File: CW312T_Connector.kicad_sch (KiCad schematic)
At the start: 1 part, among them P1 PCIEx4 EDGE CONNECTOR

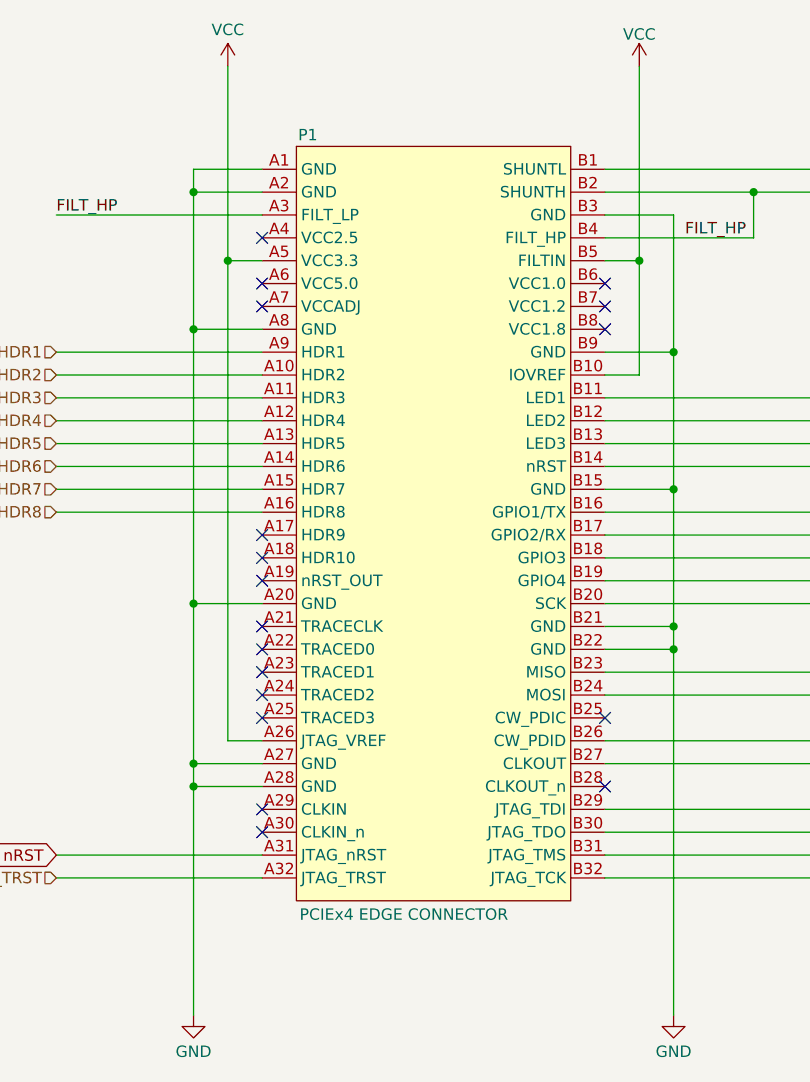
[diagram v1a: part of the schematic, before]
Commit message: updated schematic and pcb after library re-organization
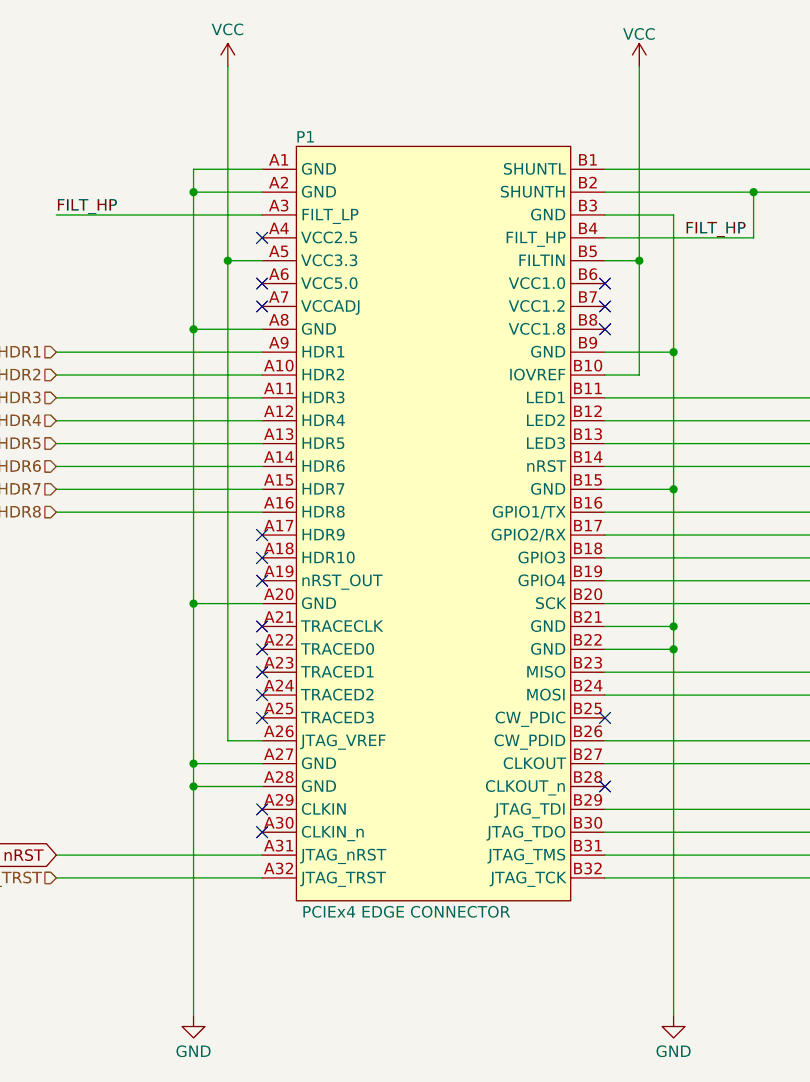
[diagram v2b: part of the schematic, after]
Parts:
- removed P1: PCIEx4 EDGE CONNECTOR, tutorial_2_library:CW312_Template, symbol tutorial_2_library:CW312T-Template
- added P1: PCIEx4 EDGE CONNECTOR, tutorial_2_library:CW312_Template, symbol NAE_Connectors:CW312T-Template
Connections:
- net CLKIN: now also P1.B27 (CLKOUT)
- net CS: now also P1.B26 (CW_PDID)
- net GND: now also P1.A1 (GND), P1.A2 (GND), P1.A20 (GND), P1.A27 (GND), P1.A28 (GND), P1.A8 (GND), P1.B15 (GND), P1.B21 (GND), P1.B22 (GND), P1.B3 (GND), P1.B9 (GND)
- net GPIO1_TX: now also P1.B16 (GPIO1/TX)
- net GPIO2_RX: now also P1.B17 (GPIO2/RX)
- net GPIO3: now also P1.B18 (GPIO3)
- net GPIO4: now also P1.B19 (GPIO4)
- net HDR1: now also P1.A9 (HDR1)
- net HDR2: now also P1.A10 (HDR2)
- net HDR3: now also P1.A11 (HDR3)
- net HDR4: now also P1.A12 (HDR4)
- net HDR5: now also P1.A13 (HDR5)
- net HDR6: now also P1.A14 (HDR6)
- net HDR7: now also P1.A15 (HDR7)
- net HDR8: now also P1.A16 (HDR8)
- net JTAG_TCK: now also P1.B32 (JTAG_TCK)
- net JTAG_TDI: now also P1.B29 (JTAG_TDI)
- net JTAG_TDO: now also P1.B30 (JTAG_TDO)
- net JTAG_TMS: now also P1.B31 (JTAG_TMS)
- net JTAG_TRST: now also P1.A32 (JTAG_TRST)
- net LED1: now also P1.B11 (LED1)
- net LED2: now also P1.B12 (LED2)
- net LED3: now also P1.B13 (LED3)
- net MISO: now also P1.B23 (MISO)
- net MOSI: now also P1.B24 (MOSI)
- net SCK: now also P1.B20 (SCK)
- net SHUNTH: now also P1.A3 (FILT_LP), P1.B2 (SHUNTH), P1.B4 (FILT_HP)
- net SHUNTL: now also P1.B1 (SHUNTL)
- net VCC: now also P1.A26 (JTAG_VREF), P1.A5 (VCC3.3), P1.B10 (IOVREF), P1.B5 (FILTIN)
- net nRST: now also P1.A31 (JTAG_nRST), P1.B14 (nRST)
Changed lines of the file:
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@@
+	)
+	(symbol
+		(lib_id "NAE_Connectors:CW312T-Template")
+		(at 128.27 49.53 0)
+		(unit 1)
+		(exclude_from_sim no)
+		(in_bom no)
+		(on_board yes)
+		(dnp no)
+		(property "Reference" "P1"
+			(at 114.046 45.974 0)
+			(effects
+				(font
+					(size 1.27 1.27)
+				)
+			)
+		)
+		(property "Value" "PCIEx4 EDGE CONNECTOR"
+			(at 125.222 132.08 0)
+			(effects
+				(font
+					(size 1.27 1.27)
+				)
+			)
+		)
+		(property "Footprint" "tutorial_2_library:CW312_Template"
+			(at 124.46 142.24 0)
+			(effects
+				(font
+					(size 1.27 1.27)
+				)
+				(hide yes)
+			)
+		)
+		(property "Datasheet" ""
+			(at 125.73 48.26 0)
+			(effects
+				(font
+					(size 1.27 1.27)
+				)
+				(hide yes)
+			)
+		)
+		(property "Description" "BOARD AND EDGE CONNECTOR TEMPLATE FOR CW312 TARGETS"
+			(at 137.16 138.43 0)
+			(effects
+				(font
+					(size 1.27 1.27)
+				)
+				(hide yes)
+			)
+		)
+		(pin "A18"
+		)
+		(pin "A20"
+		)
+		(pin "A24"
+		)
+		(pin "A19"
+		)
+		(pin "A11"
+		)
+		(pin "A2"
+		)
+		(pin "A17"
+		)
+		(pin "A25"
+		)
+		(pin "A27"
+		)
+		(pin "A21"
+		)
+		(pin "A28"
+		)
+		(pin "A29"
+		)
+		(pin "A3"
+		)
+		(pin "A30"
+		)
+		(pin "A31"
+		)
+		(pin "A13"
+		)
+		(pin "A32"
+		)
+		(pin "A4"
+		)
+		(pin "A22"
+		)
+		(pin "A23"
+		)
+		(pin "A26"
+		)
+		(pin "A5"
+		)
+		(pin "A6"
+		)
+		(pin "B2"
+		)
+		(pin "A10"
+		)
+		(pin "A1"
+		)
+		(pin "A12"
+		)
+		(pin "A14"
+		)
+		(pin "A15"
+		)
+		(pin "A16"
+		)
+		(pin "A7"
+		)
+		(pin "B31"
+		)
+		(pin "B7"
+		)
+		(pin "B24"
+		)
+		(pin "B17"
+		)
+		(pin "B12"
+		)
+		(pin "B29"
+		)
+		(pin "B13"
+		)
+		(pin "B4"
+		)
+		(pin "B6"
+		)
+		(pin "B15"
+		)
+		(pin "B23"
+		)
+		(pin "B27"
+		)
+		(pin "B18"
+		)
+		(pin "B11"
+		)
+		(pin "B28"
+		)
+		(pin "A9"
+		)
+		(pin "B14"
+		)
+		(pin "B21"
+		)
+		(pin "B25"
+		)
+		(pin "B26"
+		)
+		(pin "B5"
+		)
+		(pin "B22"
+		)
+		(pin "B8"
+		)
+		(pin "B9"
+		)
+		(pin "B16"
+		)
+		(pin "B20"
+		)
+		(pin "A8"
+		)
+		(pin "B1"
+		)
+		(pin "B19"
+		)
+		(pin "B3"
+		)
+		(pin "B10"
+		)
+		(pin "B30"
+		)
+		(pin "B32"
+		)
+		(instances
+			(project ""
+				(path "/ece4ddd9-bce6-488f-8cc3-9727cdb2c227/8c7b6d59-2095-41d5-a8e3-3e94e254f14b"
+					(reference "P1")
+					(unit 1)
+				)
+			)
+		)
 	)
 	(symbol
@@
 					(unit 1)
 				)
-			)
-		)
-	)
-	(symbol
-		(lib_id "tutorial_2_library:CW312T-Template")
-		(at 128.27 49.53 0)
-		(unit 1)
-		(exclude_from_sim no)
-		(in_bom no)
-		(on_board yes)
-		(dnp no)
-		(property "Reference" "P1"
-			(at 114.3 45.72 0)
-			(effects
-				(font
-					(size 1.27 1.27)
-				)
-			)
-		)
-		(property "Value" "PCIEx4 EDGE CONNECTOR"
-			(at 124.968 132.334 0)
-			(effects
-				(font
-					(size 1.27 1.27)
-				)
-			)
-		)
-		(property "Footprint" "tutorial_2_library:CW312_Template"
-			(at 124.46 142.24 0)
-			(effects
-				(font
-					(size 1.27 1.27)
-				)
-				(hide yes)
-			)
-		)
-		(property "Datasheet" ""
-			(at 125.73 48.26 0)
-			(effects
-				(font
-					(size 1.27 1.27)
-				)
-				(hide yes)
-			)
-		)
-		(property "Description" "BOARD AND EDGE CONNECTOR TEMPLATE FOR CW312 TARGETS"
-			(at 137.16 138.43 0)
-			(effects
-				(font
-					(size 1.27 1.27)
-				)
-				(hide yes)
-			)
-		)
-		(pin "A6"
-		)
-		(pin "B17"
-		)
-		(pin "B2"
-		)
-		(pin "B11"
-		)
-		(pin "B21"
-		)
-		(pin "A20"
-		)
-		(pin "A21"
-		)
-		(pin "A3"
-		)
-		(pin "A10"
-		)
-		(pin "A29"
-		)
-		(pin "A22"
-		)
-		(pin "B13"
-		)
-		(pin "B15"
-		)
-		(pin "B22"
-		)
-		(pin "B23"
-		)
-		(pin "B25"
-		)
-		(pin "B29"
-		)
-		(pin "B5"
-		)
-		(pin "A13"
-		)
-		(pin "A11"
-		)
-		(pin "A17"
-		)
-		(pin "A4"
-		)
-		(pin "A30"
-		)
-		(pin "B1"
-		)
-		(pin "A2"
-		)
-		(pin "A23"
-		)
-		(pin "B28"
-		)
-		(pin "B31"
-		)
-		(pin "B8"
-		)
-		(pin "A12"
-		)
-		(pin "A1"
-		)
-		(pin "B30"
-		)
-		(pin "B4"
-		)
-		(pin "B26"
-		)
-		(pin "A9"
-		)
-		(pin "A5"
-		)
-		(pin "B12"
-		)
-		(pin "A18"
-		)
-		(pin "B24"
-		)
-		(pin "B27"
-		)
-		(pin "B6"
-		)
-		(pin "B3"
-		)
-		(pin "A26"
-		)
-		(pin "A19"
-		)
-		(pin "A28"
-		)
-		(pin "A7"
-		)
-		(pin "B16"
-		)
-		(pin "B20"
-		)
-		(pin "B32"
-		)
-		(pin "A8"
-		)
-		(pin "B7"
-		)
-		(pin "A27"
-		)
-		(pin "A31"
-		)
-		(pin "A32"
-		)
-		(pin "B19"
-		)
-		(pin "A15"
-		)
-		(pin "B14"
-		)
-		(pin "A24"
-		)
-		(pin "B10"
-		)
-		(pin "A25"
-		)
-		(pin "A16"
-		)
-		(pin "B18"
-		)
-		(pin "A14"
-		)
-		(pin "B9"
-		)
-		(instances
-			(project ""
-				(path "/ece4ddd9-bce6-488f-8cc3-9727cdb2c227/8c7b6d59-2095-41d5-a8e3-3e94e254f14b"
-					(reference "P1")
-					(unit 1)
-				)
